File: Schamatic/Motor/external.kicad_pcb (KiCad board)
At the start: 2 copper layers, 45 x 45 mm, 49 parts, among them J1 CONN_02X05, J11 V, J12 U, J13 W, J3 RS485, J6 12, J9 GND, Q1 PSMN3R3-40YS, Q2 PSMN3R3-40YS, Q3 PSMN3R3-40YS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

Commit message: USART frequencies match
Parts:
- moved U4 1.20 mm to (65.5, 71.7)
- moved U3 1.07 mm to (70.9, 65.5)
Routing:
- net +3V3: track 38.7 -> 40.2 mm
- net CS: track 45.1 -> 46.4 mm
- net MISO: track 45.3 -> 46.3 mm
- net Net-(C9-Pad1): track 12.4 -> 13.0 mm
- net MOSI: track 42.3 -> 42.9 mm
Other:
- outline, holes or cut-outs redrawn

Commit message: high voltage controller
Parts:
- removed the REF** at (81.0, 81.0)
- removed the REF** at (50.0, 81.0)
- removed the REF** at (81.0, 50.0)
- removed the REF** at (50.0, 50.0)
- added C11: 4.7uF, Capacitors_SMD:C_1206, F.Cu at (73.7, 48.5)
- added C12: 0.1uF, Capacitors_SMD:C_0603, F.Cu at (67.3, 60.3)
- added L2: 220uH, Inductors_SMD:L_1210, F.Cu at (69.8, 45.3)
- added R10: 237K, Capacitors_SMD:C_0603, F.Cu at (59.6, 48.5)
- added R11: 10K, Capacitors_SMD:C_0603, F.Cu at (81.3, 62.4)
- added R12: 230K, Capacitors_SMD:C_0603, F.Cu at (69.8, 47.8)
- added R13: 10K, Capacitors_SMD:C_0603, F.Cu at (69.8, 48.9)
- added R14: 1Ohm, Capacitors_SMD:C_0603, F.Cu at (72.6, 46.0)
- added REF**: Hole-m3, Dizzy:Hole-m3, F.Cu at (50.2, 79.0)
- added REF**: Hole-m3, Dizzy:Hole-m3, F.Cu at (81.2, 79.0)
- added REF**: Hole-m3, Dizzy:Hole-m3, F.Cu at (81.2, 48.0)
- added REF**: Hole-m3, Dizzy:Hole-m3, F.Cu at (50.2, 48.0)
- C1: footprint Capacitors_SMD:C_0805 -> Capacitors_SMD:C_1210
- C10: value 0.1uF -> 0.01uF
- C3: value 1uF -> 2uF; footprint Capacitors_SMD:C_1206 -> Capacitors_SMD:C_1210
- C9: value 0.1uF -> 1uF
- U4: value A1335 -> LM5019; footprint Housings_SSOP:TSSOP-14_4.4x5mm_Pitch0.65mm -> Housings_DFN_QFN:DFN-8-1EP_4x4mm_Pitch0.8mm
- moved C9 28.8 mm to (66.9, 47.9), turned to 270 degrees
- moved C10 26.6 mm to (66.9, 45.2)
- moved U4 25.8 mm to (62.9, 46.0), turned to 0 degrees
- moved L1 6.69 mm to (74.5, 55.4), turned to 0 degrees
- moved D1 6.63 mm to (73.3, 59.6)
- moved C1 6.11 mm to (73.7, 51.4)
- moved C2 5.75 mm to (71.5, 55.9)
- moved U1 5.75 mm to (65.6, 55.6)
- moved Y1 5.75 mm to (69.0, 60.8)
- moved C5 4.47 mm to (58.9, 54.1)
- moved C6 4.46 mm to (58.8, 52.1)
- moved C4 4.14 mm to (58.9, 55.8)
- moved C3 1.33 mm to (57.9, 45.7), turned to 90 degrees
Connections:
- C10 pad 1: +3V3 -> Net-(C10-Pad1)
- C10 pad 2: Earth -> Net-(C10-Pad2)
- C3 pad 1: VM -> Net-(C3-Pad1)
- D4 pad 1: VM -> Net-(C3-Pad1)
- U2 pad 2: Earth -> DE
- U4 pad 2: Net-(C9-Pad1) -> Net-(C3-Pad1)
- U4 pad 3: Earth -> Net-(C3-Pad1)
- U4 pad 4: (no net) -> Net-(R10-Pad1)
- U4 pad 5: +3V3 -> Net-(R12-Pad2)
- U4 pad 6: (no net) -> Net-(C9-Pad1)
- U4 pad 7: Earth -> Net-(C10-Pad1)
- U4 pad 8: Net-(C9-Pad1) -> Net-(C10-Pad2)
- U4 pad 9: (no net) -> Earth
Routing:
- net +3V3: track 40.2 -> 102.0 mm, vias 15 -> 12
- net MISO: track 46.3 -> 22.5 mm, vias 3 -> 2
- net SCK: track 43.2 -> 19.5 mm, vias 3 -> 2
- net Earth: track 4.57 -> 28.0 mm, vias 0 -> 8
- net CS: track 46.4 -> 25.3 mm, vias 3 -> 2
- net MOSI: track 42.9 -> 25.0 mm, vias 3 -> 2
- net DE: track 48.3 -> 33.3 mm
- net RX: track 38.7 -> 23.9 mm
- net TX: track 37.3 -> 23.8 mm
- net SWDCLK: track 24.2 -> 36.2 mm
- net Net-(C9-Pad1): track 13.0 -> 2.26 mm
- net Net-(CALIB1-Pad1): track 37.9 -> 28.1 mm
- net Net-(C3-Pad1): track 0.00 -> 9.67 mm
- net O1: track 25.9 -> 34.7 mm
- net SWDIO: track 22.1 -> 29.2 mm
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- added copper zone on B.Cu, net Earth
- removed copper zone on B.Cu, net +3V3
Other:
- board text added: "Calib"
- board text added: "ID"

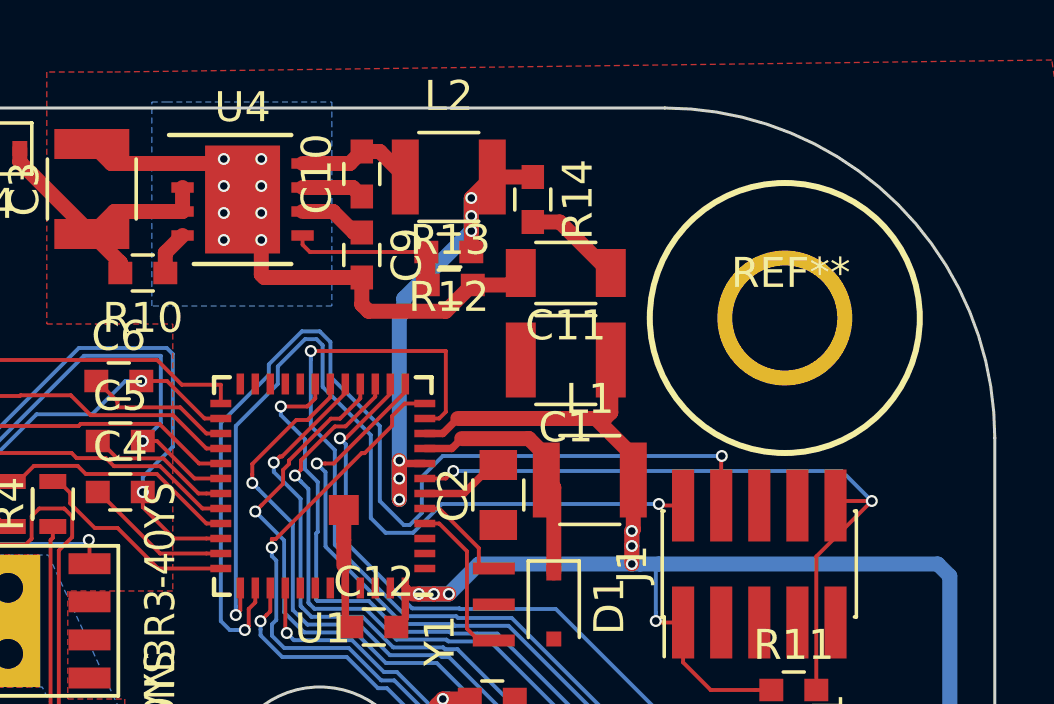
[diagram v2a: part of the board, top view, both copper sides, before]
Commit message: this was failed attempt to increase voltage
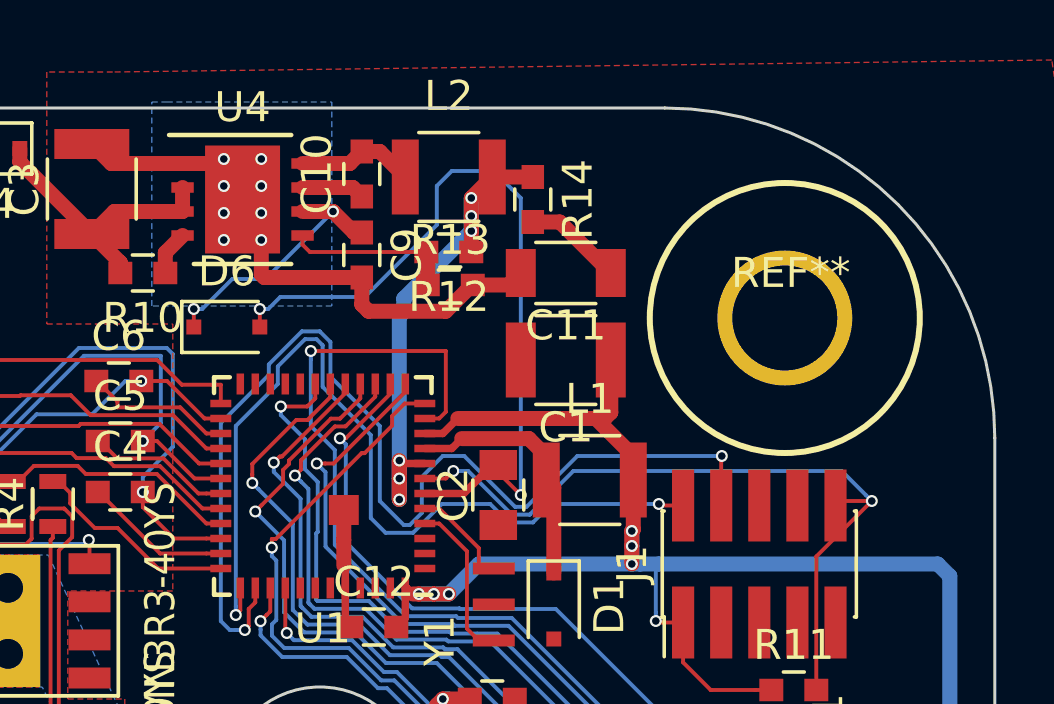
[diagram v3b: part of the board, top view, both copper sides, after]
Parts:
- added D6: D_Small, Diodes_SMD:D_SOD-323F, F.Cu at (62.4, 50.3)
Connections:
- net Net-(C2-Pad2) renamed VREG_12
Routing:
- net VREG_12: track 2.84 -> 26.4 mm, vias 0 -> 2
- net Net-(C9-Pad1): track 2.26 -> 8.85 mm, vias 0 -> 2
- net SWDCLK: track 36.2 -> 37.6 mm
- net NRST: track 24.6 -> 25.8 mm
- net SWDIO: track 29.2 -> 29.7 mm
